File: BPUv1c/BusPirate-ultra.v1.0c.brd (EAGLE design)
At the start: 100 x 50 mm, 187 parts, among them J1 USB-C-12, J2 CON_HEADER_1X04, J3 CON_HEADER_1X10-RIGHT_ANGLED_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, J4 CON_MOLEX_MALE_SMT_SH_1.25, Q300 PMV65XP, Q301 DMMT3906W, U100 STM32F103ZX, U101 W25X40CL, U200 74HCT4067, U201 MCP6001, U202 ADS7041, U300 MCP1824_ADJ, U301 MCP6001, U302 MCP1700, U303 MCP1801T-1202I/OT, U400 SN74LVC1T45DBV, U401 SN74LVC1T45DBV, U402 74LVC1G07DBV, U403 74LVC1G07DBV, U404 SN74LVC1T45DBV, U405 SN74LVC1T45DBV, U406 74LVC1G07DBV, U407 74LVC1G07DBV, U408 SN74LVC1T45DBV, U409 SN74LVC1T45DBV, U410 74LVC1G07DBV, U411 74LVC1G07DBV, U412 SN74LVC1T45DBV, U413 SN74LVC1T45DBV, U414 74LVC1G07DBV, U415 74LVC1G07DBV, U500 74HCT4066PW, U501 74HCT4066PW, U600 23LC1024, U601 23LC1024, U602 74LVC245A, U700 ICE40HX4K

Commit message: renamed DISPLAY_AUX2 to DISPLAY_AUX1 connected to PB1 renamed DISPLAY_AUX1 to DISPLAY_RESET and connected to PB2/BOOT1, wired a pull down resistor too rewired DISPLAY_CS from PF11 to PC4 rewired DISPLAY_D/P from PB1 to PC5 wired FSMC_A6/PF12 to FPGA pin 42 renamed MCU_AUX9 to FSMC_A7 renamed MCU_AUX11 to FSMC_A8 renamed MCU_AUX12 to FSMC_A9 renamed MCU_AUX10 to FSMC_A10 and move it to FSMC_A10/PG0 wired PG1/MCU_INT2 to FPGA pin 114
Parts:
- added R101: 10K, dp_devices.v6:R402
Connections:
- net MCU_AUX11 renamed FSMC_A8
- net MCU_AUX12 renamed FSMC_A9
- net MCU_AUX9 renamed FSMC_A7
- removed net DISPLAY_AUX2: J4.P4, U100.45
- removed net MCU_AUX10: U100.57, U700.38
- new net DISPLAY_RESET: J4.P5, R101.2, U100.48
- new net FSMC_A10: U100.56, U700.38
- new net FSMC_A6: U100.50, U700.42
- new net MCU_INT2: U100.57, U700.114
- new net N$10: U100.49
- net DISPLAY_AUX1: now also J4.P4, U100.47; no longer J4.P5, U100.44
- net DISPLAY_CS: now also U100.44; no longer U100.49
- net DISPLAY_D/P: now also U100.45; no longer U100.47
- net GND: now also R101.1; no longer U100.48
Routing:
- net MCU_AUX10: track 29.4 -> 0.00 mm, vias 2 -> 0
- net FSMC_A10: track 0.00 -> 23.9 mm, vias 0 -> 2
- net DISPLAY_AUX2: track 11.6 -> 0.00 mm
- net DISPLAY_RESET: track 0.00 -> 6.65 mm
- net DISPLAY_AUX1: track 11.3 -> 7.59 mm
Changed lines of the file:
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@@
 <element name="U302" library="dp_devices.v6" package="SOT-89" value="MCP1700" x="-25.908" y="-44.958"/>
 <element name="U200" library="dp_devices.v6" package="TSSOP-24" value="74HCT4067" x="-25.4" y="-55.626"/>
+<element name="R101" library="dp_devices.v6" package="R402" value="10K" x="-28.194" y="-62.23"/>
 </elements>
 <signals>
@@
 <contactref element="J3" pad="10"/>
 <contactref element="U201" pad="2"/>
-<contactref element="U100" pad="48"/>
 <contactref element="U100" pad="138"/>
 <contactref element="R308" pad="2"/>
@@
 <contactref element="U200" pad="12"/>
 <contactref element="C200" pad="1"/>
+<contactref element="R101" pad="1"/>
 <wire x1="90.85" y1="41.115" x2="99.1121" y2="41.1833" width="0" layer="19" extent="1-1"/>
 <wire x1="84.9884" y1="41.671" x2="90.85" y2="41.115" width="0" layer="19" extent="1-1"/>
@@
 <wire x1="1.1684" y1="12.6746" x2="3.214" y2="12.7" width="0" layer="19" extent="1-1"/>
 <wire x1="1.2446" y1="8.8237" x2="3.214" y2="10.8204" width="0" layer="19" extent="1-1"/>
-<wire x1="22.785" y1="14.25" x2="19.4564" y2="16.4846" width="0" layer="19" extent="1-1"/>
-<wire x1="24.285" y1="14.25" x2="22.785" y2="14.25" width="0" layer="19" extent="1-1"/>
-<wire x1="23.7998" y1="16.4846" x2="24.285" y2="14.25" width="0" layer="19" extent="1-1"/>
-<wire x1="25.019" y1="10.834" x2="24.285" y2="14.25" width="0" layer="19" extent="1-1"/>
 <wire x1="8.636" y1="11.811" x2="11.908" y2="14.351" width="0" layer="19" extent="16-16"/>
 <wire x1="2.6" y1="20.68" x2="6.78" y2="20.68" width="0" layer="19" extent="1-1"/>
+<wire x1="23.7998" y1="16.4846" x2="19.4564" y2="16.4846" width="0" layer="19" extent="1-1"/>
+<wire x1="24.285" y1="14.25" x2="23.7998" y2="16.4846" width="0" layer="19" extent="1-1"/>
+<wire x1="25.019" y1="10.834" x2="24.285" y2="14.25" width="0" layer="19" extent="1-1"/>
 <wire x1="29.845" y1="10.834" x2="25.019" y2="10.834" width="0" layer="19" extent="1-1"/>
 <wire x1="29.285" y1="14.25" x2="29.845" y2="10.834" width="0" layer="19" extent="1-1"/>
@@
 <wire x1="-27.408" y1="-46.608" x2="-15.406" y2="-47.498" width="0" layer="19" extent="1-1"/>
 <wire x1="-21.84" y1="-58.5438" x2="-15.406" y2="-47.498" width="0" layer="19" extent="1-1"/>
+<wire x1="-28.844" y1="-62.23" x2="-21.84" y2="-58.5438" width="0" layer="19" extent="1-1"/>
 </signal>
 <signal name="3V3">
@@
 <wire x1="18.9305625" y1="39.878" x2="18.9305625" y2="40.9683" width="0.254" layer="16"/>
 </signal>
-<signal name="MCU_AUX9">
+<signal name="FSMC_A7">
 <contactref element="U700" pad="37"/>
 <contactref element="U100" pad="53"/>
@@
 <wire x1="44.323" y1="14.478" x2="32.512" y2="14.478" width="0.254" layer="16"/>
 </signal>
-<signal name="MCU_AUX10">
+<signal name="FSMC_A10">
 <contactref element="U700" pad="38"/>
 <wire x1="45.8393" y1="14.25" x2="45.8393" y2="14.9937" width="0.254" layer="1"/>
@@
 <wire x1="30.2927375" y1="19.685" x2="27.305" y2="19.685" width="0.254" layer="16"/>
 <wire x1="27.305" y1="19.685" x2="26.924" y2="20.066" width="0.254" layer="16"/>
-<contactref element="U100" pad="57"/>
-<wire x1="27.285" y1="14.25" x2="27.285" y2="19.705" width="0.254" layer="1"/>
 <wire x1="27.285" y1="19.705" x2="26.924" y2="20.066" width="0.254" layer="1"/>
+<contactref element="U100" pad="56"/>
+<wire x1="26.785" y1="14.25" x2="31.71986875" y2="15.90513125" width="0" layer="19" extent="1-16"/>
 </signal>
-<signal name="MCU_AUX11">
+<signal name="FSMC_A8">
 <contactref element="U700" pad="39"/>
 <wire x1="46.3393" y1="14.25" x2="46.3393" y2="15.2853375" width="0.254" layer="1"/>
@@
 <wire x1="27.051" y1="21.082" x2="24.511" y2="21.082" width="0.254" layer="16"/>
 </signal>
-<signal name="MCU_AUX12">
+<signal name="FSMC_A9">
 <contactref element="U700" pad="41"/>
 <wire x1="47.3393" y1="14.25" x2="47.3393" y2="15.3987" width="0.254" layer="1"/>
@@
 <wire x1="23.785" y1="10.38813125" x2="29.501" y2="4.67213125" width="0.254" layer="1"/>
 <wire x1="29.501" y1="4.67213125" x2="29.501" y2="4.477" width="0.254" layer="1"/>
-<contactref element="U100" pad="49"/>
-<wire x1="23.785" y1="10.38813125" x2="23.285" y2="14.25" width="0" layer="19" extent="1-1"/>
+<contactref element="U100" pad="44"/>
+<wire x1="23.785" y1="10.38813125" x2="20.785" y2="14.25" width="0" layer="19" extent="1-1"/>
 </signal>
 <signal name="DISPLAY_D/P">
@@
 <wire x1="23.285" y1="10.205" x2="28.251" y2="5.239" width="0.254" layer="1"/>
 <wire x1="28.251" y1="5.239" x2="28.251" y2="4.477" width="0.254" layer="1"/>
-<contactref element="U100" pad="47"/>
-<wire x1="23.285" y1="10.205" x2="22.285" y2="14.25" width="0" layer="19" extent="1-1"/>
+<contactref element="U100" pad="45"/>
+<wire x1="23.285" y1="10.205" x2="21.285" y2="14.25" width="0" layer="19" extent="1-1"/>
 </signal>
 <signal name="DISPLAY_PWM">
@@
 <contactref element="U100" pad="80"/>
 </signal>
-<signal name="DISPLAY_AUX2">
-<contactref element="U100" pad="45"/>
+<signal name="DISPLAY_AUX1">
+<contactref element="U100" pad="47"/>
 <contactref element="J4" pad="P4"/>
-<wire x1="21.285" y1="14.25" x2="21.285" y2="10.213" width="0.254" layer="1"/>
 <wire x1="21.285" y1="10.213" x2="25.751" y2="5.747" width="0.254" layer="1"/>
 <wire x1="25.751" y1="5.747" x2="25.751" y2="4.477" width="0.254" layer="1"/>
-</signal>
-<signal name="DISPLAY_AUX1">
-<contactref element="U100" pad="44"/>
-<contactref element="J4" pad="P5"/>
-<wire x1="20.785" y1="14.25" x2="20.785" y2="9.59" width="0.254" layer="1"/>
-<wire x1="20.785" y1="9.59" x2="24.501" y2="5.874" width="0.254" layer="1"/>
-<wire x1="24.501" y1="5.874" x2="24.501" y2="4.477" width="0.254" layer="1"/>
+<wire x1="21.285" y1="10.213" x2="22.285" y2="14.25" width="0" layer="19" extent="1-1"/>
 </signal>
 <signal name="D-">
@@
 <contactref element="U700" pad="52"/>
 </signal>
+<signal name="DISPLAY_RESET">
+<contactref element="U100" pad="48"/>
+<contactref element="R101" pad="2"/>
+<contactref element="J4" pad="P5"/>
+<wire x1="20.785" y1="9.59" x2="24.501" y2="5.874" width="0.254" layer="1"/>
+<wire x1="24.501" y1="5.874" x2="24.501" y2="4.477" width="0.254" layer="1"/>
+<wire x1="24.501" y1="4.477" x2="-27.544" y2="-62.23" width="0" layer="19" extent="1-1"/>
+<wire x1="22.785" y1="14.25" x2="20.785" y2="9.59" width="0" layer="19" extent="1-1"/>
+</signal>
+<signal name="N$10">
+<contactref element="U100" pad="49"/>
+</signal>
+<signal name="FSMC_A6">
+<contactref element="U100" pad="50"/>
+<contactref element="U700" pad="42"/>
+<wire x1="23.785" y1="14.25" x2="47.8393" y2="14.25" width="0" layer="19" extent="1-1"/>
+</signal>
+<signal name="MCU_INT2">
+<contactref element="U100" pad="57"/>
+<contactref element="U700" pad="114"/>
+<wire x1="27.285" y1="14.25" x2="60.3393" y2="35.75" width="0" layer="19" extent="1-1"/>
+</signal>
 </signals>

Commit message: rewiring of v1c schematic continues
renamed MCU_AUX7 to MCU_INT0
renamed MCU_AUX8 to MCU_INT1
renamed MCU_INT0 to MCU_PWM0
renamed PWM to MCU_PWM1
moved LAT_OE to FPGA pin 96
moved LAT_DIR to FPGA pin 95
moved LAT_0 to FPGA pin 94
moved LAT_1 to FPGA pin 93
moved LAT_2 to FPGA pin 91
moved LAT_3 to FPGA pin 90
moved LAT_4 to FPGA pin 88
moved LAT_5 to FPGA pin 87
moved LAT_6 to FPGA pin 85
moved LAT_7 to FPGA pin 84
moved ADC_MUX S0 to FPGA pin 80
moved ADC_MUX S1 to FPGA pin 81
moved ADC_MUX S2 to FPGA pin 82
moved ADC_MUX S3 to FPGA pin 83
renamed DISPLAY_D/P to DISPLAY_AUX1
renamed DISPLAY_AUX2 to DISPLAY_D/P
added 220R series resistors to each BPIOs
wired ADC_MUX_EN to FPGA pin 55, since pin 114 is already MCU_INT2
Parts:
- added R424, R425, R426, R427, R428, R429, R430, R431: 220R, dp_devices.v6:R402
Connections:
- net PWM renamed MCU_PWM1
- removed net MCU_AUX7: U100.141, U700.124
- removed net MCU_AUX8: U100.142, U700.122
- new net BPIO0I: R404.2, R424.2, U400.4, U402.4
- new net BPIO1I: R410.2, R425.2, U404.4, U406.4
- new net BPIO2I: R416.2, R426.2, U408.4, U410.4
- new net BPIO3I: R422.2, R427.2, U412.4, U414.4
- new net BPIO4I: R405.2, R428.2, U401.4, U403.4
- new net BPIO5I: R411.2, R429.2, U405.4, U407.4
- new net BPIO6I: R417.2, R430.2, U409.4, U411.4
- new net BPIO7I: R423.2, R431.2, U413.4, U415.4
- new net MCU_INT1I: U100.99, U700.115
- new net MCU_PWM0: U100.102, U700.129
- net ADC_MUX_EN: now also U700.55; no longer U700.96
- net ADC_MUX_S0: now also U700.80; no longer U700.93
- net ADC_MUX_S1: now also U700.81; no longer U700.94
- net ADC_MUX_S2: now also U700.82; no longer U700.95
- net ADC_MUX_S3: now also U700.83
- net BPIO0: now also R424.1; no longer R404.2, U400.4, U402.4
- net BPIO1: now also R425.1; no longer R410.2, U404.4, U406.4
- net BPIO2: now also R426.1; no longer R416.2, U408.4, U410.4
- net BPIO3: now also R427.1; no longer R422.2, U412.4, U414.4
- net BPIO4: now also R428.1; no longer R405.2, U401.4, U403.4
- net BPIO5: now also R429.1; no longer R411.2, U405.4, U407.4
- net BPIO6: now also R430.1; no longer R417.2, U409.4, U411.4
- net BPIO7: now also R431.1; no longer R423.2, U413.4, U415.4
- net DISPLAY_AUX1: now also J4.P2; no longer J4.P4
- net DISPLAY_CS: now also U100.49; no longer U100.44
- net DISPLAY_D/P: now also J4.P4; no longer J4.P2
- net LAT0: now also U700.94; no longer U700.91
- net LAT1: now also U700.93; no longer U700.90
- net LAT2: now also U700.91; no longer U700.88
- net LAT3: now also U700.90; no longer U700.87
- net LAT4: now also U700.88; no longer U700.85
- net LAT5: now also U700.87; no longer U700.84
- net LAT6: now also U700.85; no longer U700.83
- net LAT7: now also U700.84; no longer U700.82
- net LAT_DIR: now also U700.95; no longer U700.81
- net LAT_OE: now also U700.96; no longer U700.80
- net MCU_INT0: now also U100.141, U700.124; no longer U100.102, U700.129
- net MCU_INT1: now also U100.142, U700.122; no longer U100.99, U700.115
- net N$10: now also U100.44; no longer U100.49
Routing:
- net MCU_INT1: track 0.00 -> 51.7 mm, vias 0 -> 2
- net MCU_AUX8: track 51.7 -> 0.00 mm, vias 2 -> 0
- net MCU_AUX7: track 48.5 -> 0.00 mm, vias 2 -> 0
- net MCU_PWM0: track 0.00 -> 33.8 mm, vias 0 -> 2
- net ADC_MUX_EN: track 27.1 -> 0.00 mm
- net LAT_OE: track 11.3 -> 37.3 mm
- net ADC_MUX_S2: track 19.8 -> 0.00 mm
- net ADC_MUX_S1: track 19.1 -> 0.00 mm
- net LAT_DIR: track 11.7 -> 30.4 mm
- net ADC_MUX_S0: track 18.4 -> 0.00 mm
- net LAT1: track 3.64 -> 19.7 mm
- net LAT0: track 3.59 -> 19.1 mm
- net MCU_INT0: track 33.8 -> 48.5 mm
- net BPIO4I: track 0.00 -> 14.4 mm, vias 0 -> 2
- net BPIO4: track 51.7 -> 37.2 mm, vias 3 -> 1
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
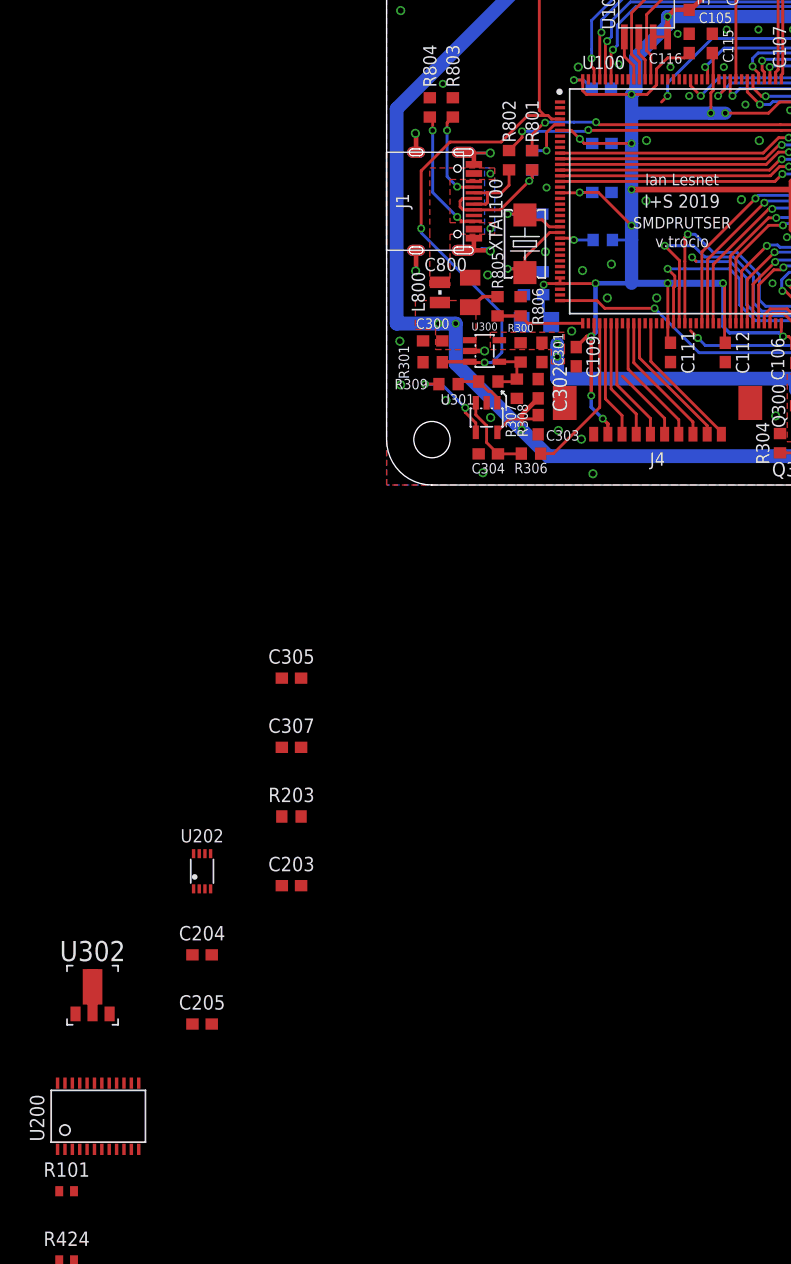
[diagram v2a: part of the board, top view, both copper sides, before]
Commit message: continued on v1c schematic changes renamed MCU_AUX4 to MCU_INT3 and move it from MCU PD6 to PD2 renamed MCU_INT1I to MCU_AUX0 fix display connections
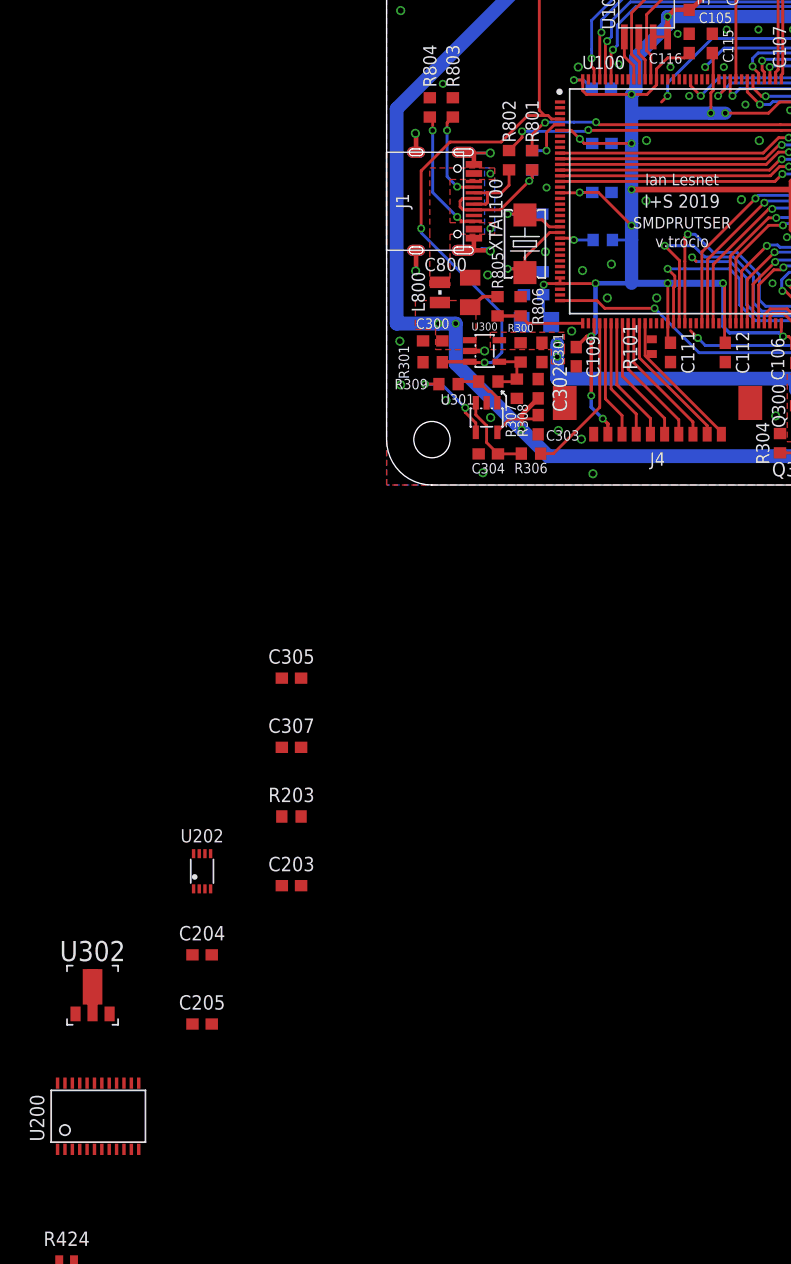
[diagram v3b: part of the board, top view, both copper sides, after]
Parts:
- moved R101 90.5 mm to (23.4, 12.2), turned to 90 degrees
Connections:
- net MCU_INT1I renamed MCU_AUX0
- removed net MCU_AUX4: U100.122, U700.134
- removed net N$10: U100.44
- removed net N$29: U100.116
- new net DISPLAY_CSI: U100.49
- new net MCU_INT3: U100.116, U700.134
- net DISPLAY_CS: now also J4.P5, U100.44; no longer J4.P1, U100.49
- net DISPLAY_RESET: now also J4.P1; no longer J4.P5
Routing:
- net MCU_AUX4: track 25.6 -> 0.00 mm, vias 2 -> 0
- net MCU_INT3: track 0.00 -> 24.7 mm, vias 0 -> 2
- net DISPLAY_RESET: track 6.65 -> 12.6 mm
- net DISPLAY_CS: track 12.3 -> 11.3 mm

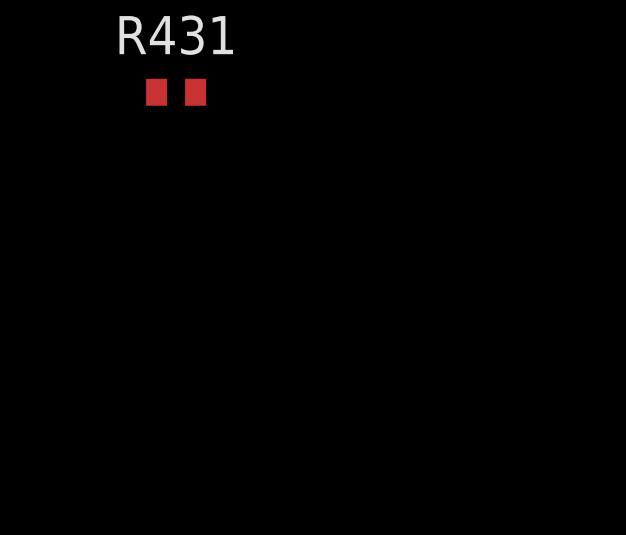
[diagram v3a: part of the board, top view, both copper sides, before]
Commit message: continue on v1c schematic revisions -removed net DISPLAY_CSI on MCU pin 49 -renamed MCU_AUX5 to MCU_AUX4 and MCU_AUX6 to MCU_AUX5 -renamed MCU_ADC5 to MCU_ADC2 -renamed MCU_ADC6 to MCU_ADC3 -wired MCU_ADC0 to PA0 probing U300 output, with 2 voltage divider resistors
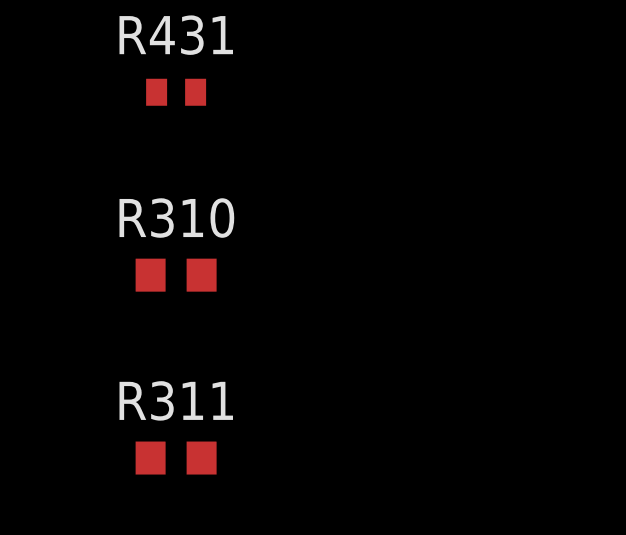
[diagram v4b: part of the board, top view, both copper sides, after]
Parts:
- added R310, R311: 10K, dp_devices.v6:R603
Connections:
- net MCU_ADC5 renamed MCU_ADC3
- net MCU_ADC6 renamed MCU_ADC2
- removed net DISPLAY_CSI: U100.49
- removed net MCU_AUX6: U100.140, U700.125
- new net MCU_ADC0: R310.2, R311.1, U100.34
- new net MCU_AUX4: U100.139, U700.130
- net GND: now also R311.2
- net MCU_AUX5: now also U100.140, U700.125; no longer U100.139, U700.130
- net N$26: now also R310.1
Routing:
- net MCU_AUX6: track 46.5 -> 0.00 mm, vias 2 -> 0
- net MCU_AUX4: track 0.00 -> 43.1 mm, vias 0 -> 2
- net MCU_AUX5: track 43.1 -> 46.5 mm

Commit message: finishing up routing on v1c board
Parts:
- C100, C101, C102, C103, C106, C108, C109, C110, C111, C112, C114, C200, C201, C202, C203, C204, C205, C302, C303, C308, C501, C602, C702, C703, C704, C705, C707, C709, C711, C712, C713, C714, C715: device dp_devices.v6:C603 -> dp_devices.v6:C402
- R100, R200, R201, R202, R203, R204, R300, R301, R307, R308, R309, R310, R311, R700, R701, R702, R800, R801, R802, R803, R804, R805, R806: device dp_devices.v6:R603 -> dp_devices.v6:R402
- moved R426 159.5 mm to (84.6, 32.3), turned to 90 degrees
- moved R430 158.7 mm to (84.6, 6.73), turned to 270 degrees
- moved R427 157.3 mm to (74.8, 32.3), turned to 90 degrees
- moved R424 157.0 mm to (84.6, 40.9), turned to 90 degrees
- moved R431 156.3 mm to (74.7, 6.73), turned to 270 degrees
- moved R428 156.0 mm to (84.6, 15.1), turned to 270 degrees
- moved R425 154.5 mm to (74.7, 40.9), turned to 90 degrees
- moved R429 153.5 mm to (74.7, 15.1), turned to 270 degrees
- moved R311 143.2 mm to (16.5, 12.8), turned to 90 degrees
- moved R310 134.4 mm to (15.9, 9.91)
- moved U200 133.5 mm to (81.0, 24.9), turned to 90 degrees
- moved U302 92.3 mm to (9.14, 40.4)
- moved C205 86.2 mm to (50.0, 7.62)
- moved C204 77.8 mm to (47.2, 3.56), turned to 180 degrees
- moved U202 75.3 mm to (47.0, 6.86), turned to 180 degrees
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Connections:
- net ADC_CLOCK: now also U700.48; no longer U700.47
- net ADC_DATA: now also U700.47; no longer U700.48
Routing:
- net MCU_INT2: track 0.00 -> 56.7 mm, vias 0 -> 2
- net ADC_MUX_EN: track 0.00 -> 33.6 mm, vias 0 -> 2
- net 1V2: track 82.6 -> 115.4 mm
- net N$47: track 0.00 -> 32.3 mm, vias 0 -> 2
- net 3V3: track 588.2 -> 620.1 mm, vias 65 -> 64
- net FSMC_A6: track 0.00 -> 28.8 mm, vias 0 -> 2
- net MCU_AUX0: track 0.00 -> 28.6 mm, vias 0 -> 2
- net ADC_MUX_S1: track 0.00 -> 28.5 mm, vias 0 -> 2
- net LAT_OE: track 37.3 -> 11.0 mm, vias 2 -> 0
- net ADC_MUX_S0: track 0.00 -> 26.2 mm, vias 0 -> 2
- net LAT_DIR: track 30.4 -> 5.13 mm, vias 2 -> 0
- net ADC_MUX_S2: track 0.00 -> 23.8 mm, vias 0 -> 2
- net VUSB: track 257.0 -> 233.2 mm, vias 14 -> 11
- net ADC_MUX_S3: track 0.00 -> 17.6 mm, vias 0 -> 2
- net BPIO4: track 37.2 -> 52.3 mm, vias 1 -> 3
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- added copper zone on layer 15, net GND
- added copper zone on layer 2, net GND
- removed copper zone on layer 1, net 3V3
